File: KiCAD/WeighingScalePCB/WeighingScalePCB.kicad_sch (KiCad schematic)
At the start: 60 parts, among them IC1 MAX6675ISA+T, IC2 APS11753KMDALX-9PL5, J1 Conn_01x04_Pin, J2 AudioJack4, J3 Conn_01x14_Pin, J4 Battery Conn, J5 buzzer conn, Q2 NX138AKR, Q3 NX138AKR, Q4 NX138AKR, Q5 NX138AKR, T1 TouchPad, T2 TouchPad, U1 XIAO-ESP32-S3-SMD, U10 LMC555xMM, U2 HX711, U3 LMC555xMM, U4 74LVC1G79, U5 TTP223-BA6, U6 TTP223-BA6, U7 74LVC1G79, U8 74LVC1G04, U9 74LVC1G08

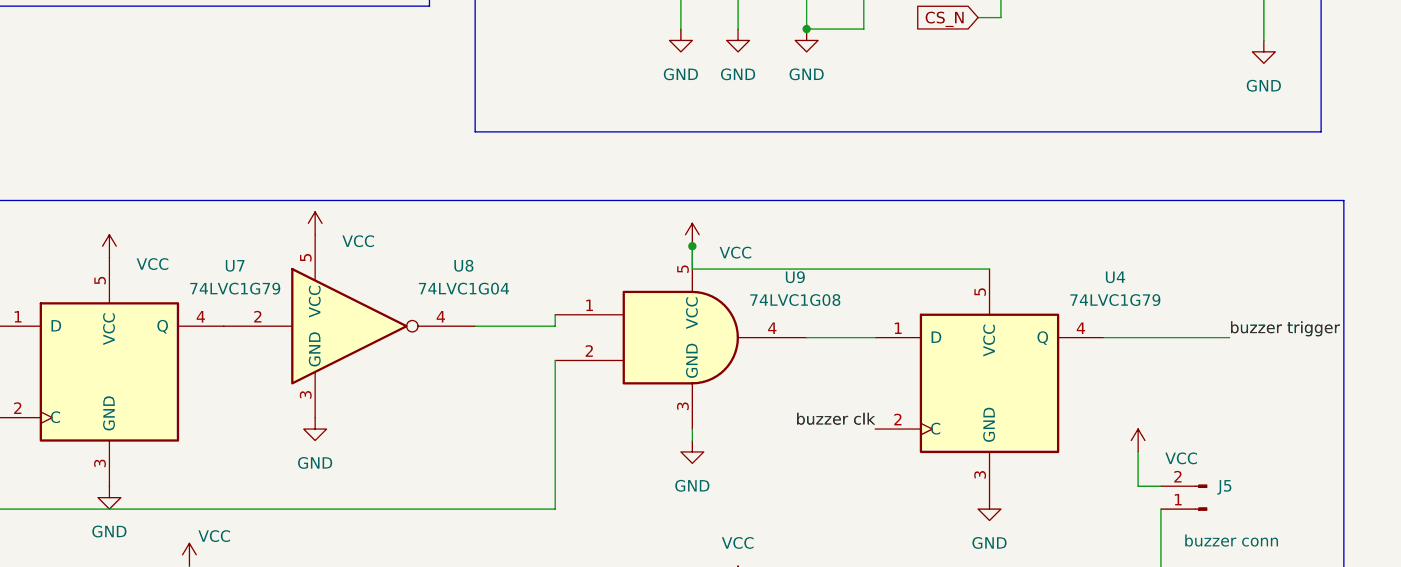
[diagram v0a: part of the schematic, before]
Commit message: added more specific p/n for d flip flop
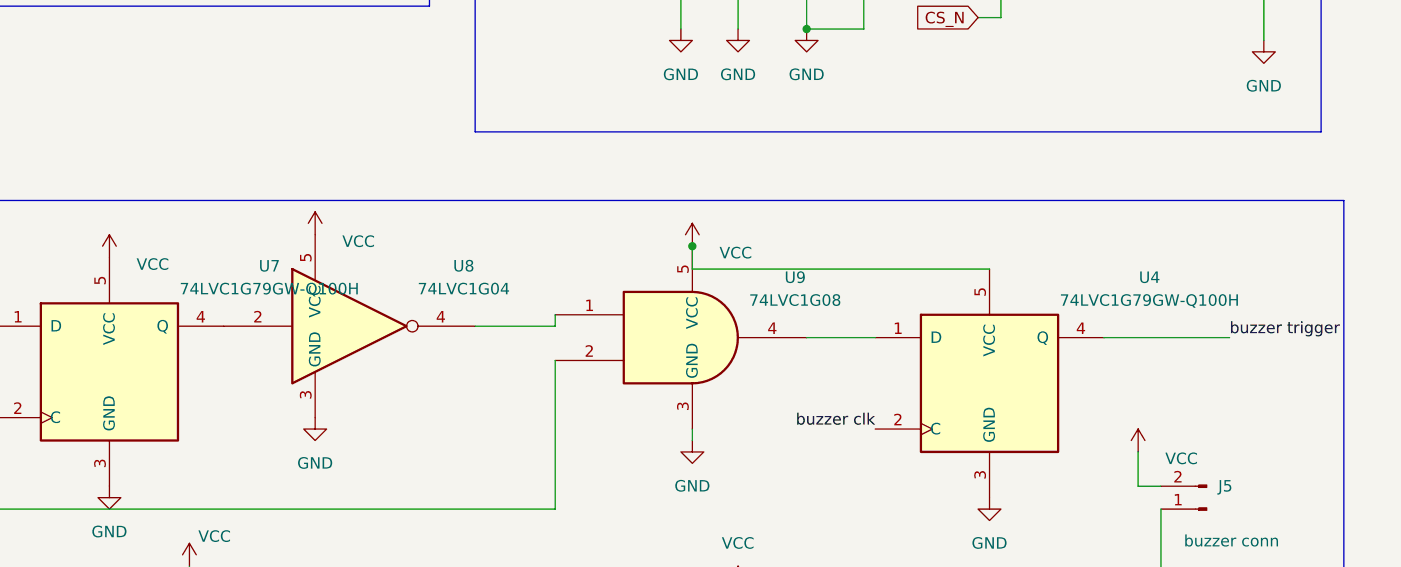
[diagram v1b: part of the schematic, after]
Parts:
- U4, U7: value 74LVC1G79 -> 74LVC1G79GW-Q100H
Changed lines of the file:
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@@
 		(fields_autoplaced yes)
 		(property "Reference" "U4"
-			(at 375.92 136.8411 0)
-			(effects
-				(font
-					(size 1.27 1.27)
-				)
-			)
-		)
-		(property "Value" "74LVC1G79"
-			(at 375.92 139.3811 0)
+			(at 379.73 136.8411 0)
+			(effects
+				(font
+					(size 1.27 1.27)
+				)
+			)
+		)
+		(property "Value" "74LVC1G79GW-Q100H"
+			(at 379.73 139.3811 0)
 			(effects
 				(font
@@
 		(fields_autoplaced yes)
 		(property "Reference" "U7"
-			(at 278.13 135.5711 0)
-			(effects
-				(font
-					(size 1.27 1.27)
-				)
-			)
-		)
-		(property "Value" "74LVC1G79"
-			(at 278.13 138.1111 0)
-			(effects
-				(font
+			(at 281.94 135.5711 0)
+			(effects
+				(font
+					(size 1.27 1.27)
+				)
+			)
+		)
+		(property "Value" "74LVC1G79GW-Q100H"
+			(at 281.94 138.1111 0)
+			(effects
+				(font

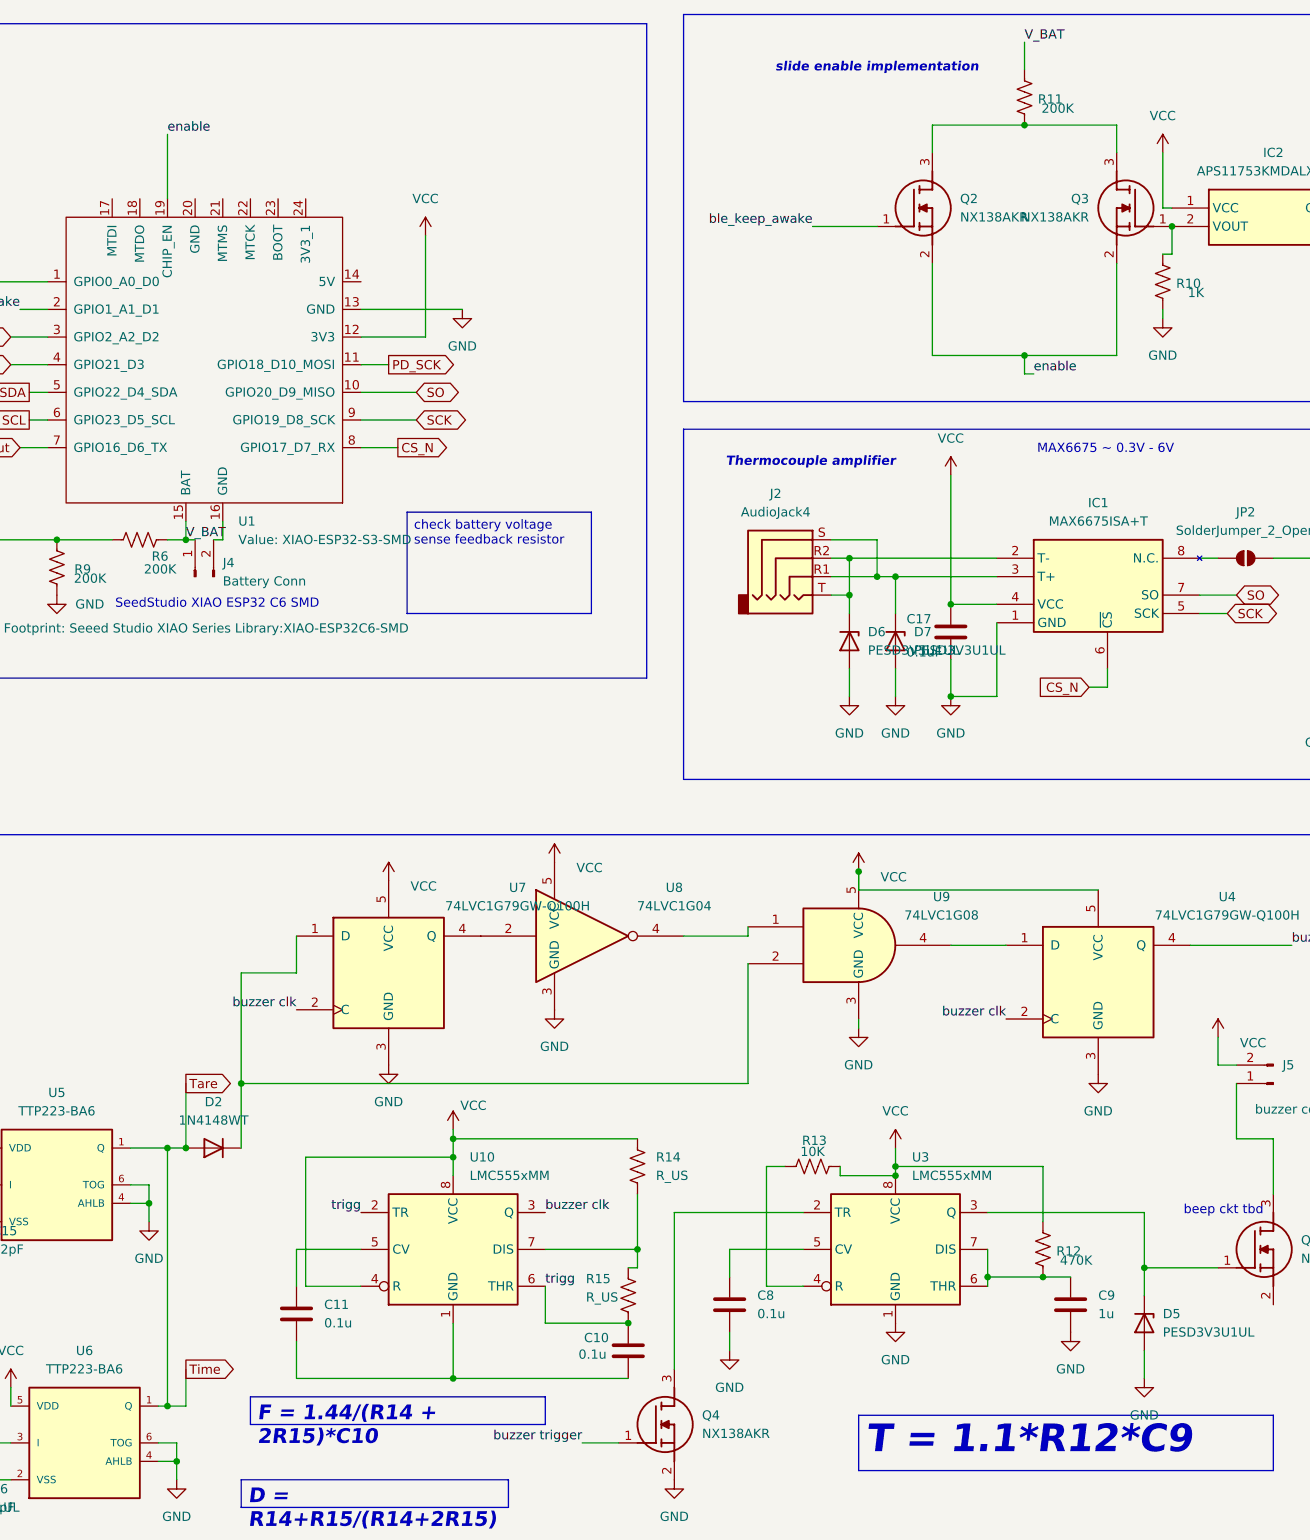
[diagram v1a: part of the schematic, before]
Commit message: Corrected time and tare orring circuit
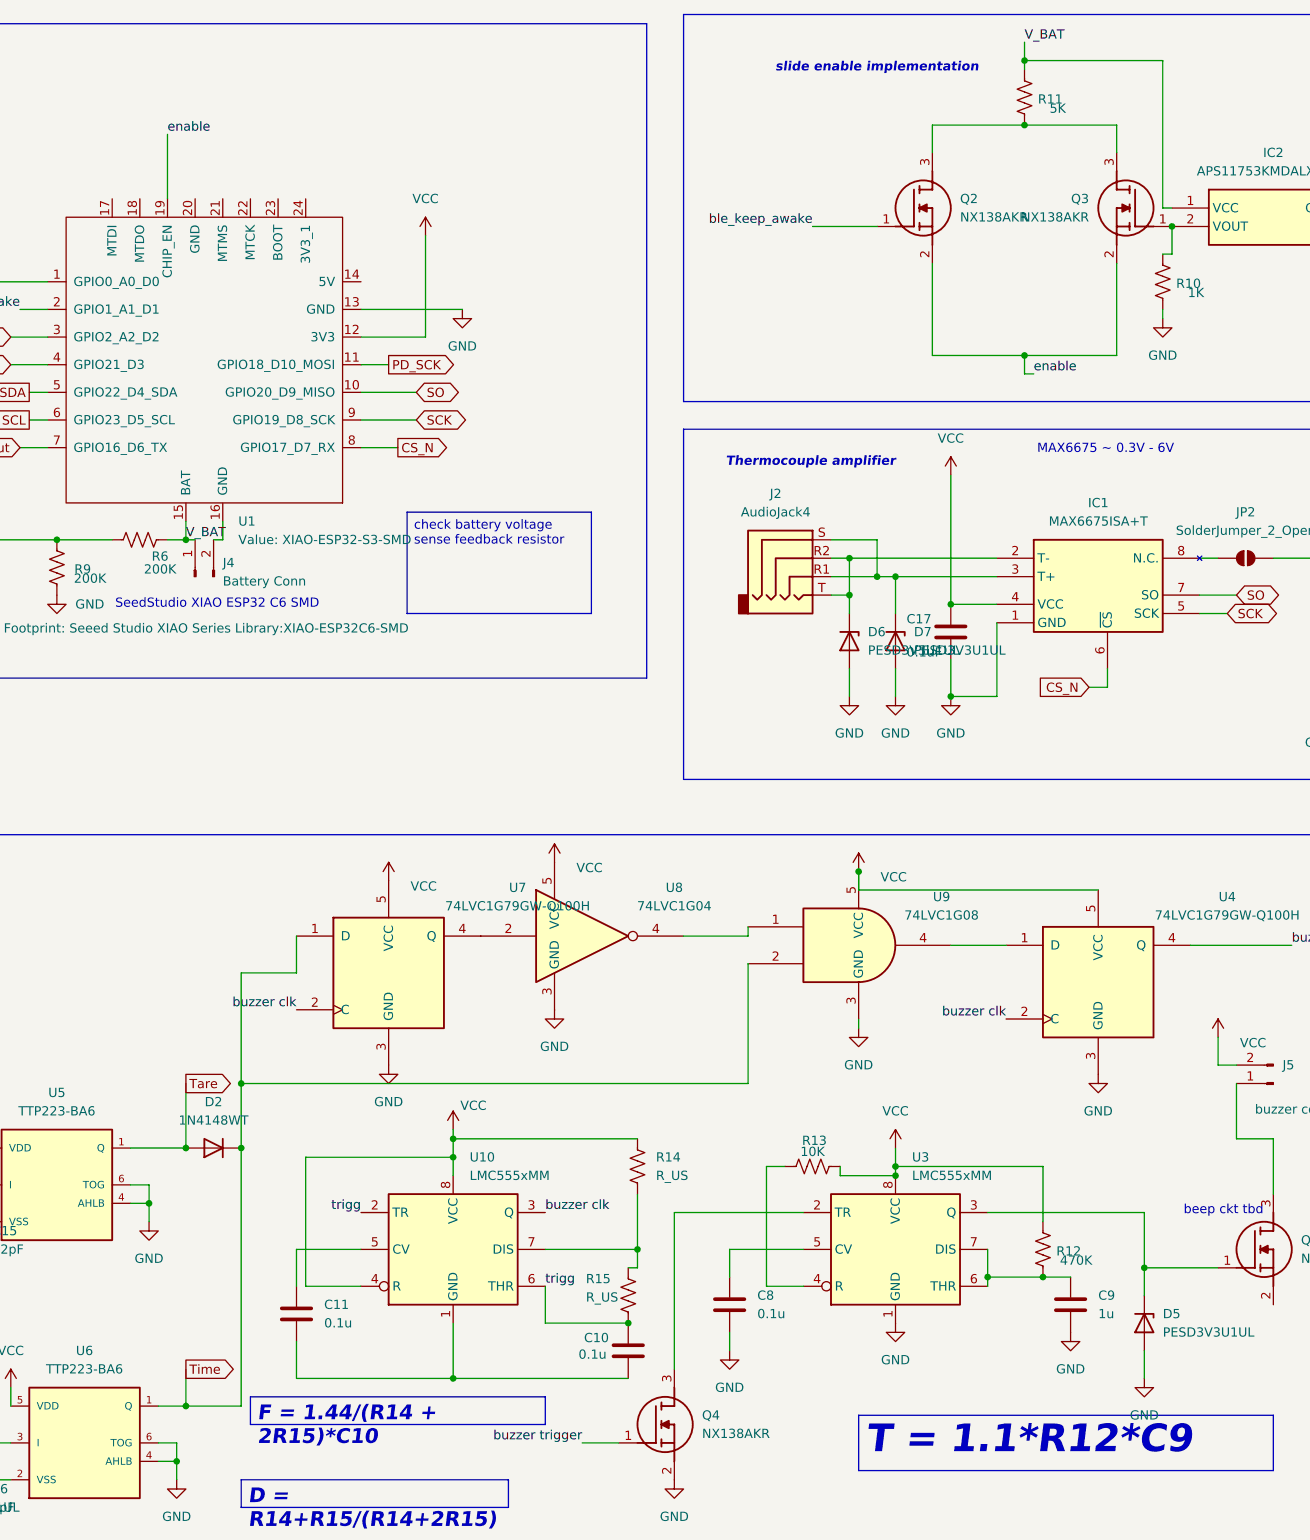
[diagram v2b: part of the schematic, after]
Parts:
- R11: value 200K -> 5K
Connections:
- net Tare: no longer U1.4 (GPIO21_D3), U6.1 (Q)
- net VCC: no longer IC2.1 (VCC)
- net V_BAT: now also IC2.1 (VCC)
- net Time: now reaches D2.1 (K), U7.1 (D), U9.2
- net Time: now also U1.4 (GPIO21_D3), U6.1 (Q)
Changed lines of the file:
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@@
 	)
 	(junction
+		(at 236.22 207.01)
+		(diameter 0)
+		(color 0 0 0 0)
+	)
+	(junction
 		(at 334.01 175.26)
 		(diameter 0)
@@
 	)
 	(junction
+		(at 351.79 21.59)
+		(diameter 0)
+		(color 0 0 0 0)
+	)
+	(junction
 		(at 234.95 214.63)
 		(diameter 0)
@@
 	)
 	(junction
-		(at 233.68 207.01)
-		(diameter 0)
-		(color 0 0 0 0)
-	)
-	(junction
 		(at 137.16 67.31)
 		(diameter 0)
@@
 	)
 	(junction
-		(at 114.3 113.03)
+		(at 243.84 171.45)
 		(diameter 0)
 		(color 0 0 0 0)
 	)
 	(junction
-		(at 351.79 30.48)
+		(at 114.3 113.03)
 		(diameter 0)
 		(color 0 0 0 0)
 	)
 	(junction
-		(at 334.01 173.99)
+		(at 351.79 30.48)
 		(diameter 0)
 		(color 0 0 0 0)
 	)
 	(junction
-		(at 218.44 87.63)
+		(at 334.01 173.99)
 		(diameter 0)
 		(color 0 0 0 0)
 	)
 	(junction
-		(at 233.68 171.45)
+		(at 218.44 87.63)
 		(diameter 0)
 		(color 0 0 0 0)
@@
 	(wire
 		(pts
-			(xy 232.41 207.01) (xy 233.68 207.01)
+			(xy 232.41 207.01) (xy 236.22 207.01)
 		)
 		(stroke
@@
 	(wire
 		(pts
-			(xy 351.79 19.05) (xy 351.79 22.86)
+			(xy 351.79 19.05) (xy 351.79 21.59)
 		)
 		(stroke
@@
 	(wire
 		(pts
-			(xy 370.84 41.91) (xy 370.84 34.29)
+			(xy 370.84 21.59) (xy 370.84 41.91)
 		)
 		(stroke
@@
 	(wire
 		(pts
-			(xy 233.68 207.01) (xy 233.68 171.45)
+			(xy 243.84 207.01) (xy 243.84 171.45)
 		)
 		(stroke
@@
 	(wire
 		(pts
+			(xy 243.84 207.01) (xy 236.22 207.01)
+		)
+		(stroke
+			(width 0)
+			(type default)
+		)
+	)
+	(wire
+		(pts
 			(xy 328.93 153.67) (xy 328.93 154.94)
 		)
@@
 	(wire
 		(pts
-			(xy 233.68 171.45) (xy 236.22 171.45)
+			(xy 313.69 146.05) (xy 313.69 162.56)
 		)
 		(stroke
@@
 	(wire
 		(pts
-			(xy 313.69 146.05) (xy 313.69 162.56)
+			(xy 102.87 50.8) (xy 102.87 39.37)
 		)
 		(stroke
@@
 	(wire
 		(pts
-			(xy 102.87 50.8) (xy 102.87 39.37)
+			(xy 198.12 223.52) (xy 198.12 227.33)
 		)
 		(stroke
@@
 	(wire
 		(pts
-			(xy 198.12 223.52) (xy 198.12 227.33)
+			(xy 375.92 97.79) (xy 379.73 97.79)
 		)
 		(stroke
@@
 	(wire
 		(pts
-			(xy 375.92 97.79) (xy 379.73 97.79)
+			(xy 351.79 21.59) (xy 351.79 22.86)
 		)
 		(stroke
@@
 	(wire
 		(pts
+			(xy 370.84 21.59) (xy 351.79 21.59)
+		)
+		(stroke
+			(width 0)
+			(type default)
+		)
+	)
+	(wire
+		(pts
 			(xy 273.05 195.58) (xy 273.05 203.2)
 		)
@@
 	(wire
 		(pts
-			(xy 233.68 207.01) (xy 236.22 207.01)
-		)
-		(stroke
-			(width 0)
-			(type default)
-		)
-	)
-	(wire
-		(pts
 			(xy 146.05 160.02) (xy 71.12 160.02)
 		)
@@
 	(wire
 		(pts
-			(xy 228.6 171.45) (xy 233.68 171.45)
+			(xy 228.6 171.45) (xy 236.22 171.45)
 		)
 		(stroke
@@
 			)
 		)
-		(property "Value" "200K"
+		(property "Value" "5K"
 			(at 356.362 28.194 0)
 			(effects
@@
 					(unit 1)
 				)
-			)
-		)
-	)
-	(symbol
-		(lib_id "power:VCC")
-		(at 370.84 34.29 0)
-		(unit 1)
-		(exclude_from_sim no)
-		(in_bom yes)
-		(on_board yes)
-		(dnp no)
-		(fields_autoplaced yes)
-		(property "Reference" "#PWR020"
-			(at 370.84 38.1 0)
-			(effects
-				(font
-					(size 1.27 1.27)
-				)
-				(hide yes)
-			)
-		)
-		(property "Value" "VCC"
-			(at 370.84 29.21 0)
-			(effects
-				(font
-					(size 1.27 1.27)
-				)
-			)
-		)
-		(property "Footprint" ""
-			(at 370.84 34.29 0)
-			(effects
-				(font
-					(size 1.27 1.27)
-				)
-				(hide yes)
-			)
-		)
-		(property "Datasheet" ""
-			(at 370.84 34.29 0)
-			(effects
-				(font
-					(size 1.27 1.27)
-				)
-				(hide yes)
-			)
-		)
-		(property "Description" "Power symbol creates a global label with name \"VCC\""
-			(at 370.84 34.29 0)
-			(effects
-				(font
-					(size 1.27 1.27)
-				)
-				(hide yes)
-			)
-		)
-		(pin "1"
-		)
-		(instances
-			(project "WeighingScalePCB"
-				(path "/fb3b7c1c-1dc1-4229-b305-25c6e0b4dbdc"
-					(reference "#PWR020")
-					(unit 1)
-				)
